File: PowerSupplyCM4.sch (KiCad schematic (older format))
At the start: 39 parts, among them J5 Screw_Terminal_01x08, Q2 SI2316BDS-T1-GE3, U2 VOMA617A, U3 VOMA617A, U4 VOMA617A

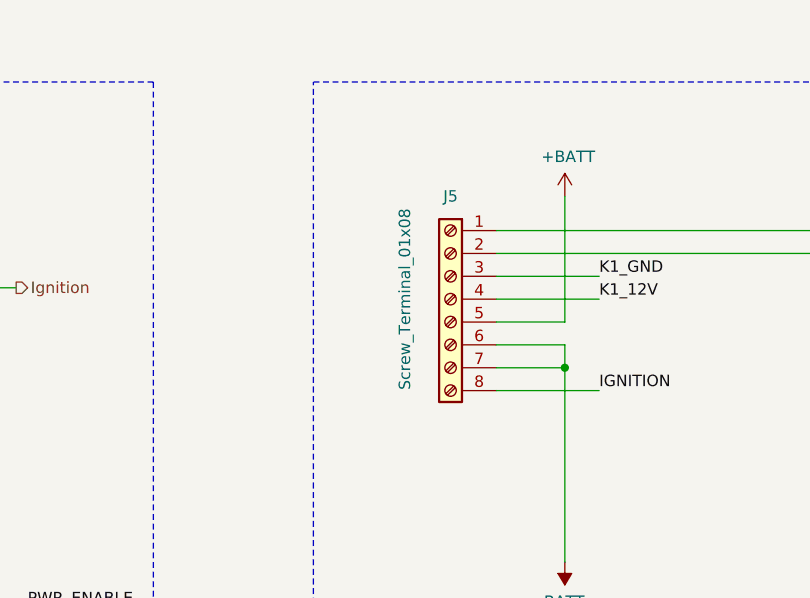
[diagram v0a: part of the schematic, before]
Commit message: - Eigene Masse Insel für Audio - Footprint Terminal PT durch PTS ersetzt (baut nur etwas tiefer)
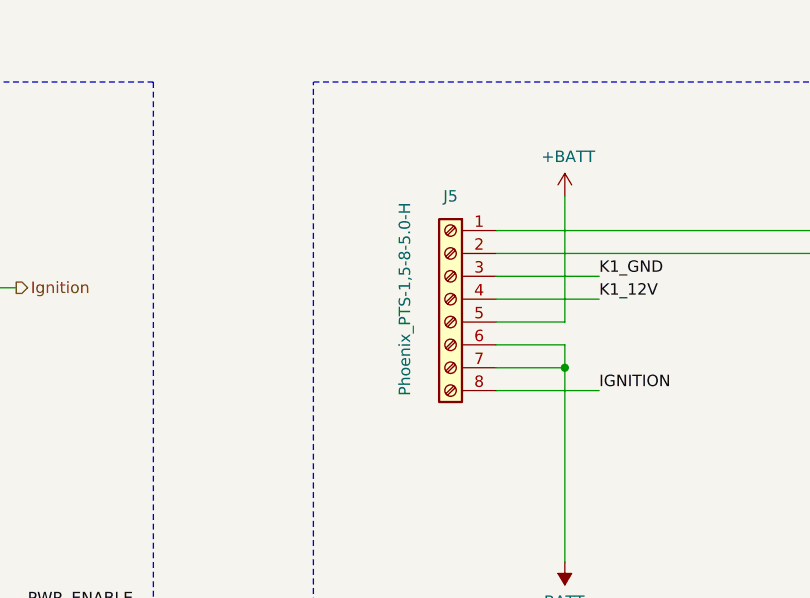
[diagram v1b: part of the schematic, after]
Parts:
- J5: value Screw_Terminal_01x08 -> Phoenix_PTS-1,5-8-5.0-H; footprint TerminalBlock_Phoenix:TerminalBlock_Phoenix_PT-1,5-8-5.0-H_1x08_P5.00mm_Horizontal -> TeKaDe:TerminalBlock_Phoenix_PTS-1,5-8-5.0-H_1x08_P5.00mm_Horizontal
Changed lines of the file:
@@
 P 11500 5600
 F 0 "J5" H 11500 6050 50  0000 C CNN
-F 1 "Screw_Terminal_01x08" V 11700 5600 50  0000 C CNN
-F 2 "TerminalBlock_Phoenix:TerminalBlock_Phoenix_PT-1,5-8-5.0-H_1x08_P5.00mm_Horizontal" H 11500 5600 50  0001 C CNN
+F 1 "Phoenix_PTS-1,5-8-5.0-H" V 11700 5600 50  0000 C CNN
+F 2 "TeKaDe:TerminalBlock_Phoenix_PTS-1,5-8-5.0-H_1x08_P5.00mm_Horizontal" H 11500 5600 50  0001 C CNN
 F 3 "~" H 11500 5600 50  0001 C CNN
 	1    11500 5600

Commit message: - BOM und Feinheiten
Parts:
- D14: value SMBJ12A-13-F -> SMBJ14A-13-F
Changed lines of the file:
@@
 Wire Wire Line
 	13500 6100 13500 6750
-$Comp
-L Device:D_Schottky D14
-U 1 1 622C78C1
-P 13500 5950
-F 0 "D14" V 13454 6029 50  0000 L CNN
-F 1 "SMBJ12A-13-F" V 13545 6029 50  0000 L CNN
-F 2 "Diode_SMD:D_SMB" H 13500 5950 50  0001 C CNN
-F 3 "~" H 13500 5950 50  0001 C CNN
-	1    13500 5950
-	0    1    1    0
-$EndComp
 Wire Notes Line
 	10900 7100 10900 4650
@@
 	1    0    0    1
 $EndComp
+$Comp
+L Device:D_Schottky D14
+U 1 1 61E6FD0C
+P 13500 5950
+F 0 "D14" V 13546 5871 50  0000 R CNN
+F 1 "SMBJ14A-13-F" V 13455 5871 50  0000 R CNN
+F 2 "Diode_SMD:D_SMB" H 13500 5950 50  0001 C CNN
+F 3 "~" H 13500 5950 50  0001 C CNN
+	1    13500 5950
+	0    1    1    0
+$EndComp
 $EndSCHEMATC

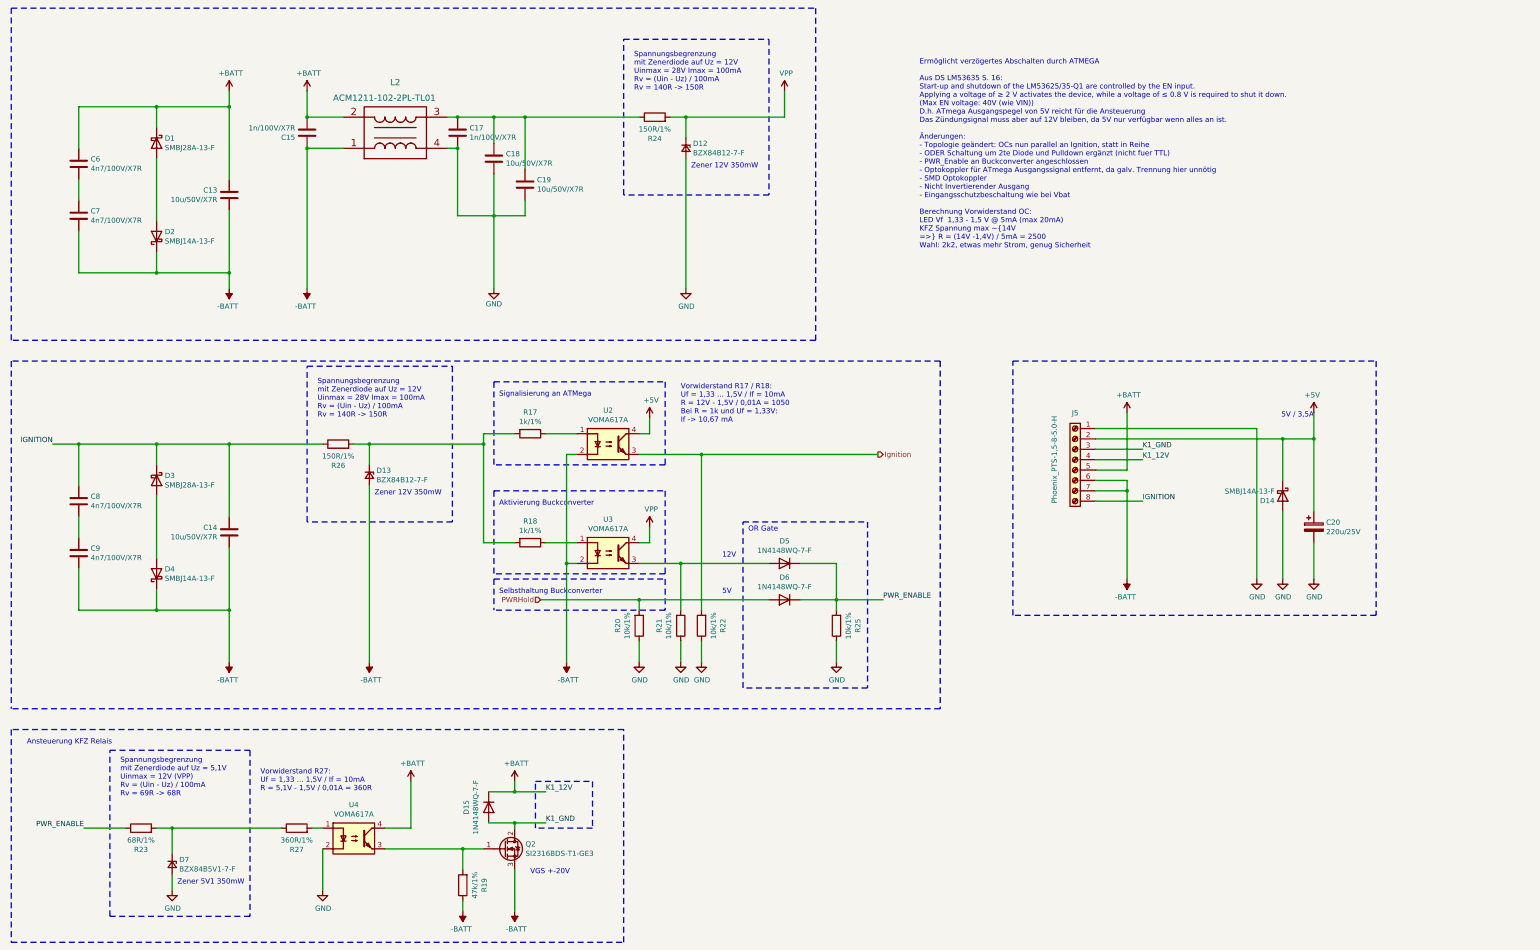
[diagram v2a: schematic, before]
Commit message: - 1,5mm Connector aus BOM gestrichen, damit ist kein Platz für Bauteile unter CM4 - RTC neben das CM4 verschoben, da mit 1,75mm um 0,25mm zu hoch für unterhalb - BT1 von THT auf SMD Typ gewechselt (Beinchen könnten Kurzschluss auf CM4 verursachen)
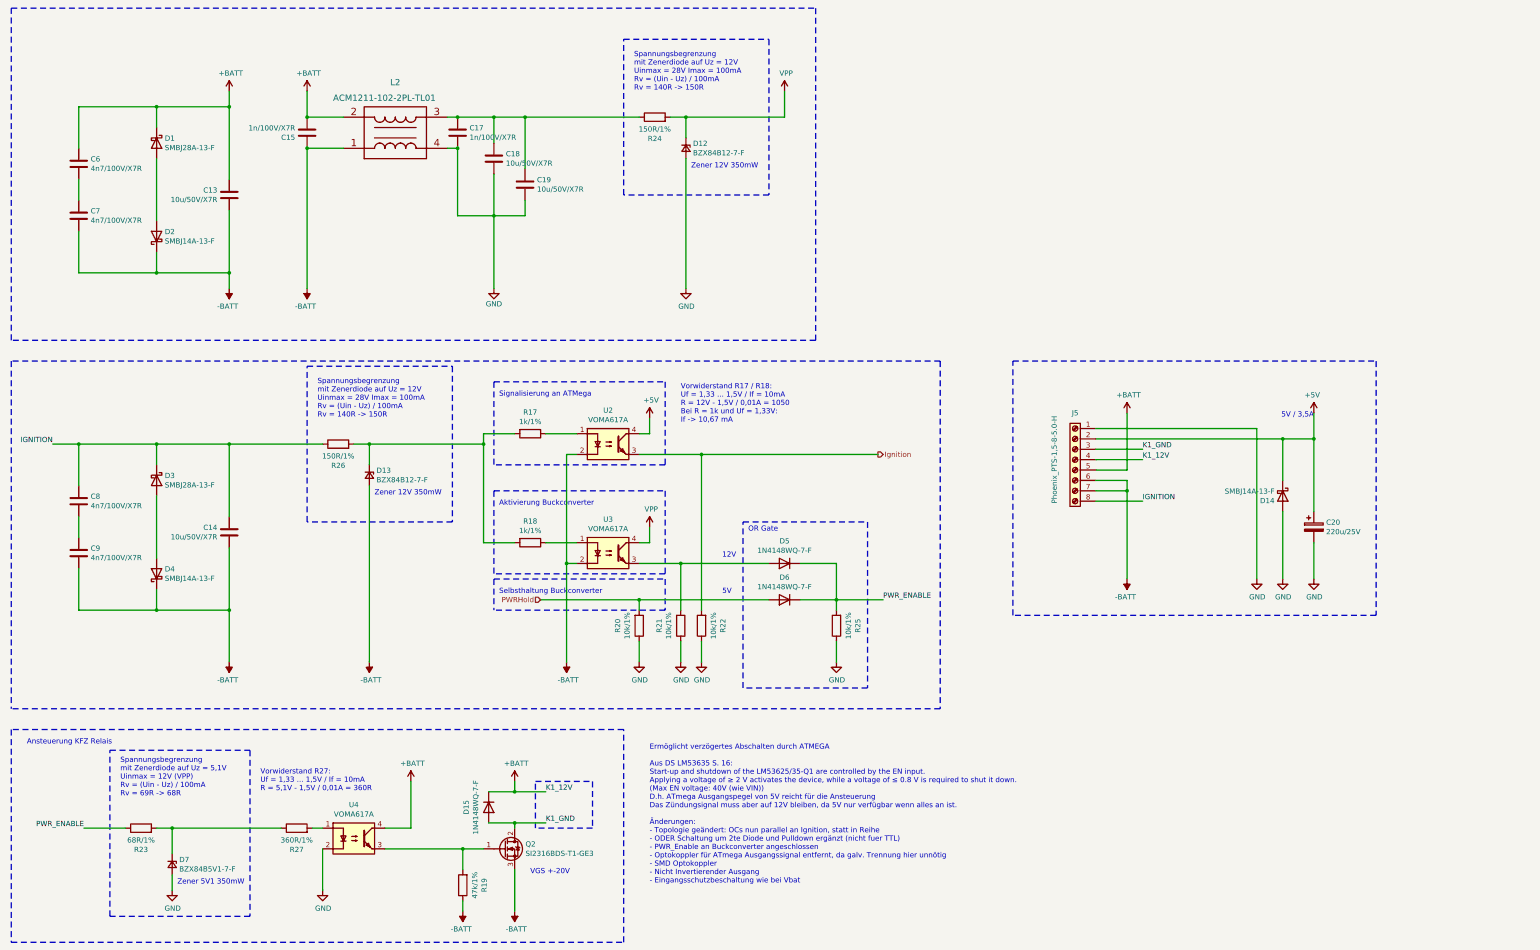
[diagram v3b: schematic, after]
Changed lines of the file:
@@
 Wire Notes Line
 	9000 1250 9000 4450
-Text Notes 10000 3650 0    50   ~ 0
-Ermöglicht verzögertes Abschalten durch ATMEGA\n\nAus DS LM53635 S. 16:\nStart-up and shutdown of the LM53625/35-Q1 are controlled by the EN input. \nApplying a voltage of ≥ 2 V activates the device, while a voltage of ≤ 0.8 V is required to shut it down. \n(Max EN voltage: 40V (wie VIN))\nD.h. ATmega Ausgangspegel von 5V reicht für die Ansteuerung\nDas Zündungsignal muss aber auf 12V bleiben, da 5V nur verfügbar wenn alles an ist.\n\nÄnderungen:\n- Topologie geändert: OCs nun parallel an Ignition, statt in Reihe\n- ODER Schaltung um 2te Diode und Pulldown ergänzt (nicht fuer TTL)\n- PWR_Enable an Buckconverter angeschlossen\n- Optokoppler für ATmega Ausgangssignal entfernt, da galv. Trennung hier unnötig\n- SMD Optokoppler\n- Nicht Invertierender Ausgang\n- Eingangsschutzbeschaltung wie bei Vbat\n\nBerechnung Vorwiderstand OC:\nLED Vf  1,33 - 1,5 V @ 5mA (max 20mA)\nKFZ Spannung max ~14V\n=> R = (14V -1,4V) / 5mA = 2500\nWahl: 2k2, etwas mehr Strom, genug Sicherheit\n\n
+Text Notes 7400 9850 0    50   ~ 0
+Ermöglicht verzögertes Abschalten durch ATMEGA\n\nAus DS LM53635 S. 16:\nStart-up and shutdown of the LM53625/35-Q1 are controlled by the EN input. \nApplying a voltage of ≥ 2 V activates the device, while a voltage of ≤ 0.8 V is required to shut it down. \n(Max EN voltage: 40V (wie VIN))\nD.h. ATmega Ausgangspegel von 5V reicht für die Ansteuerung\nDas Zündungsignal muss aber auf 12V bleiben, da 5V nur verfügbar wenn alles an ist.\n\nÄnderungen:\n- Topologie geändert: OCs nun parallel an Ignition, statt in Reihe\n- ODER Schaltung um 2te Diode und Pulldown ergänzt (nicht fuer TTL)\n- PWR_Enable an Buckconverter angeschlossen\n- Optokoppler für ATmega Ausgangssignal entfernt, da galv. Trennung hier unnötig\n- SMD Optokoppler\n- Nicht Invertierender Ausgang\n- Eingangsschutzbeschaltung wie bei Vbat\n\n\n
 Connection ~ 3350 3800
 Wire Wire Line

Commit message: [add:] annotations, corrections from testing
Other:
- note added: "-> andere Z-Diode: Spannung auf Eingangsspannung von Optokoppler reduzierbar\n -> Was hängt noch an VPP?\n -> nur Optokoppler für diskretes Or-Gate\n-> anderer Widerstand: \n - müsste deutlich geringer sein, um Z-Diode bei 12V zu halten\n - gleiches Verhalten wie derzeit, wenn Batt+ < 12V"
- note added: "Bei Ingnition low:\nI_vpp = I_batt+ = \nBei Ignition high:\nI_vpp = I_batt+ =\n"
- note added: "Footprint ist falsch \n-> falschherum eingebaut"
- note added: "U2.1: ca 0.9V kommen nur an"
- note added: "U3.1: ca 0.9V kommen nur an"
- note added: "Unzureichend um U4 zu driven\nVpp test = ca0.9V"
- note added: "Wo findet der Spannungsabfall an VPP statt?\n—> An R24 -> Warum Ist der Widerstand dahinter so gering?"
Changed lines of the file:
@@
 	0    1    1    0
 $EndComp
+Text Notes 7750 2250 0    50   Italic 0
+Unzureichend um U4 zu driven\nVpp test = ca0.9V
+Text Notes 6550 5200 0    50   Italic 0
+U2.1: ca 0.9V kommen nur an
+Text Notes 6600 6200 0    50   Italic 0
+U3.1: ca 0.9V kommen nur an
+Text Notes 9150 2500 0    50   Italic 0
+-> andere Z-Diode: Spannung auf Eingangsspannung von Optokoppler reduzierbar\n    -> Was hängt noch an VPP?\n        -> nur Optokoppler für diskretes Or-Gate\n-> anderer Widerstand: \n    - müsste deutlich geringer sein, um Z-Diode bei 12V zu halten\n    - gleiches Verhalten wie derzeit, wenn Batt+ < 12V
+Text Notes 9350 2850 0    50   Italic 0
+Wo findet der Spannungsabfall an VPP statt?\n—> An R24 -> Warum Ist der Widerstand dahinter so gering?
+Text Notes 9350 3450 0    50   Italic 0
+Bei Ingnition low:\nI_vpp = I_batt+ = \nBei Ignition high:\nI_vpp = I_batt+ =\n
+Text Notes 7450 2950 0    50   Italic 0
+Footprint ist falsch \n-> falschherum eingebaut
 $EndSCHEMATC

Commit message: all the changes before BSA21 project
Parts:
- added BT?: Battery, symbol Device:Battery
- added J?: Conn_01x08, symbol Connector_Generic:Conn_01x08
- added K?: ADW11, Relay_THT:Relay_1P1T_NO_10x24x18.8mm_Panasonic_ADW11xxxxW_THT, symbol Relay:ADW11
- added SW?: Zündung, symbol Switch:SW_DIP_x01
- added T?: Spannungswandler, symbol Device:Transformer_1P_1S
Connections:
- new net: J?.4 (Pin_4), K?.1
- new net: BT?.2 (-), J?.6 (Pin_6), J?.7 (Pin_7), K?.3
- new net: K?.5, T?.2 (AB)
- new net: J?.3 (Pin_3), K?.6
- new net: J?.1 (Pin_1), T?.3 (SA)
- new net: J?.2 (Pin_2), T?.4 (SB)
- new net: BT?.1 (+), J?.5 (Pin_5), SW?.1, T?.1 (AA)
- new net: J?.8 (Pin_8), SW?.2
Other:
- note added: "Extern\n"
- note added: "Intern\n"
- moved on the sheet: C20, D14, J5

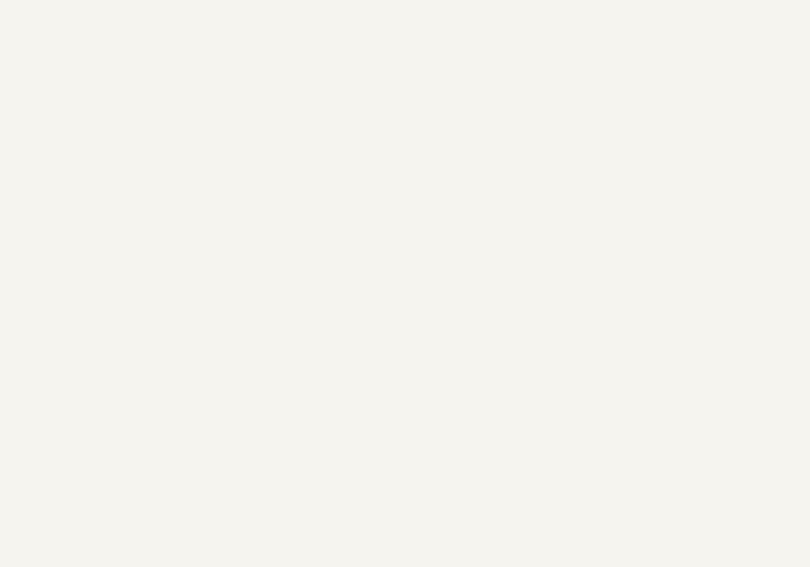
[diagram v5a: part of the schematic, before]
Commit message: schematic changes up to layout import
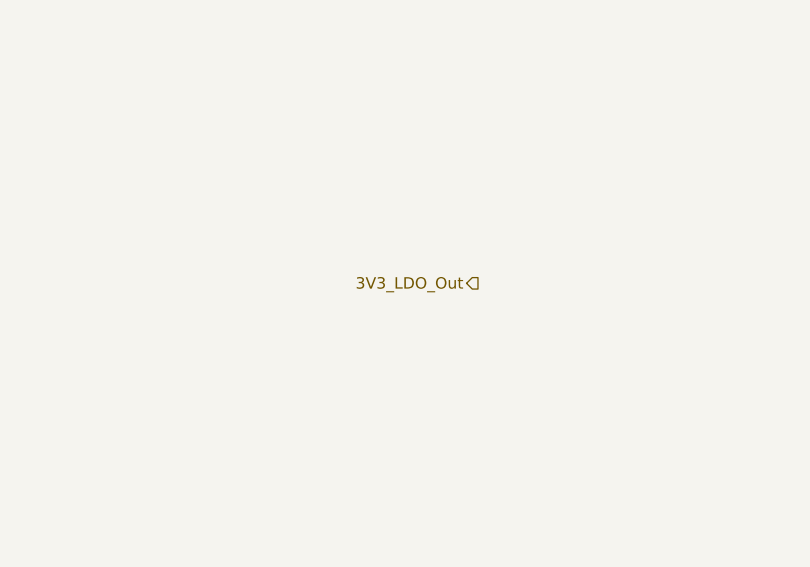
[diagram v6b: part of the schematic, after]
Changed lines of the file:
@@
 $Descr A3 16535 11693
 encoding utf-8
-Sheet 3 9
+Sheet 3 8
 Title "TIDA-00746-SchDoc"
 Date "05 06 2020"
@@
 Wire Notes Line
 	12400 7350 15900 7350
+Text HLabel 14200 2850 0    50   Output ~ 0
+3V3_LDO_Out
 $EndSCHEMATC
